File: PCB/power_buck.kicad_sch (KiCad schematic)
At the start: 6 parts

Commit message: fix: swap 3 JLCPCB-out-of-stock parts for in-stock equivalents
C_BAT1/C_BUCK_IN1/C_OLED_1/C_SYS_1/C_VIN_1 (10uF 0805 X5R 16V):
Yageo CC0805KRX5R7BB106 was at 0 stock -> HRE CGA0805X5R106K160MT
(LCSC C6119886, stock ~254k). Identical spec, different brand.

D_VBUS_TVS1: Nexperia PESD5V0S1BA,115 was down to 1 in stock -> TECH
PUBLIC TPPESD5V0S1BA (LCSC C587144, stock ~981k), a widely-stocked
pin/spec-compatible clone of the same part, same SOD-323 package.

Q_PWR1: Diodes Inc DMG2305UX-7 was down to 8 in stock -> Diodes Inc
DMG2305UX-13 (LCSC C144153, stock ~25k) -- same manufacturer, same
part, the -7/-13 suffix is just reel size (7"/13"), not an electrical
variant.

Found via live JLCPCB stock lookups after the JLCPCB upload flagged
these 3 with shortfalls. Verified via kicad-cli sch export bom and
sch erc (0 violations).

Note: PCB/snips_controller.kicad_pcb and the production/ exports still
need another Update-PCB-from-Schematic + Fabrication Toolkit pass to
pick up these changes -- not included here since they're a separate
manual step (see kicad_pcb_sync_gotcha note).

Co-Authored-By: Claude Sonnet 5 <noreply@anthropic.com>
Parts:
- C_BUCK_IN1: LCSC C2982567 -> C6119886; MF Yageo -> HRE; Manufacturer_Part_Number CC0805KRX5R7BB106 -> CGA0805X5R106K160MT
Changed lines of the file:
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@@
 			)
 		)
-		(property "MF" "Yageo"
+		(property "MF" "HRE"
 			(at 0 0 0)
 			(hide yes)
@@
 			)
 		)
-		(property "Manufacturer_Part_Number" "CC0805KRX5R7BB106"
+		(property "Manufacturer_Part_Number" "CGA0805X5R106K160MT"
 			(at 0 0 0)
 			(hide yes)
@@
 			)
 		)
-		(property "LCSC" "C2982567"
+		(property "LCSC" "C6119886"
 			(at 0 0 0)
 			(hide yes)

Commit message: task: alert on Basic-library alternatives during JLC part matching (#33)
* task: alert on Basic-library alternatives during JLC part matching

JLC's "Extended" library carries a per-unique-part setup fee on top of
unit price; "Basic" doesn't. That fee doesn't amortize well on a board
with many distinct low-quantity parts -- confirmed the hard way: our
first real JLCPCB assembly quote came back at $333.84 vs PCBWay's
~$190 for the same order, and all 33 of our matched parts were
Extended.

jlc_match.py now does a secondary search for a same-value/same-package
Basic-library part whenever the real match lands on Extended, and
flags it in the report (new BasicAlt column + a Status alert) rather
than silently leaving it. On the current board this surfaces 11
plausible Basic-library swaps (common resistor/cap values, and the
generic 1N4148W diode and 2N7002 MOSFET, which are industry-standard
parts many brands stock identically).

This is alert-only, same as the rest of this script -- it doesn't
touch the schematic. Spot-checked 4 of the 11 suggestions directly
against JLC's catalog to confirm value/package actually match, not
just a keyword hit.

Co-Authored-By: Claude Sonnet 5 <noreply@anthropic.com>

* fix: two correctness bugs in Basic-library alternative matching

1. find_basic_alternative() trusted the raw keyword-search hit without
   verifying the candidate's actual value -- JLC's fuzzy full-text search
   can return a wrong-value part that just shares digits (e.g. searching
   "100 0402" surfaced a 1kΩ resistor, EIA code "1001", as a false match
   for a 100Ω part). Now parses and compares the actual numeric value
   (with unit) before accepting a candidate; falls back to exact
   model-name matching for non-numeric values (generic diode/transistor
   part families like "1N4148W", "2N7002").

2. The new value parser's regex required the unit to be the first
   character of the string, but JLC resistor descriptions carry a
   Chinese prefix ("厚膜电阻 10kΩ ±1%" = "thi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
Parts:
- C_BUCK_IN1: LCSC C6119886 -> C15850; MF HRE -> Samsung Electro-Mechanics; Manufacturer_Part_Number CGA0805X5R106K160MT -> CL21A106KAYNNNE
- C_BUCK_OUT1: LCSC C76637 -> C45783; MF TDK -> Samsung Electro-Mechanics; Manufacturer_Part_Number C2012X5R1C226KT000E -> CL21A226MAQNNNE
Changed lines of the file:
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@@
 			)
 		)
-		(property "MF" "HRE"
+		(property "MF" "Samsung Electro-Mechanics"
 			(at 0 0 0)
 			(hide yes)
@@
 			)
 		)
-		(property "Manufacturer_Part_Number" "CGA0805X5R106K160MT"
+		(property "Manufacturer_Part_Number" "CL21A106KAYNNNE"
 			(at 0 0 0)
 			(hide yes)
@@
 			)
 		)
-		(property "LCSC" "C6119886"
+		(property "LCSC" "C15850"
 			(at 0 0 0)
 			(hide yes)
@@
 			)
 		)
-		(property "MF" "TDK"
+		(property "MF" "Samsung Electro-Mechanics"
 			(at 0 0 0)
 			(hide yes)
@@
 			)
 		)
-		(property "Manufacturer_Part_Number" "C2012X5R1C226KT000E"
+		(property "Manufacturer_Part_Number" "CL21A226MAQNNNE"
 			(at 0 0 0)
 			(hide yes)
@@
 			)
 		)
-		(property "LCSC" "C76637"
+		(property "LCSC" "C45783"
 			(at 0 0 0)
 			(hide yes)

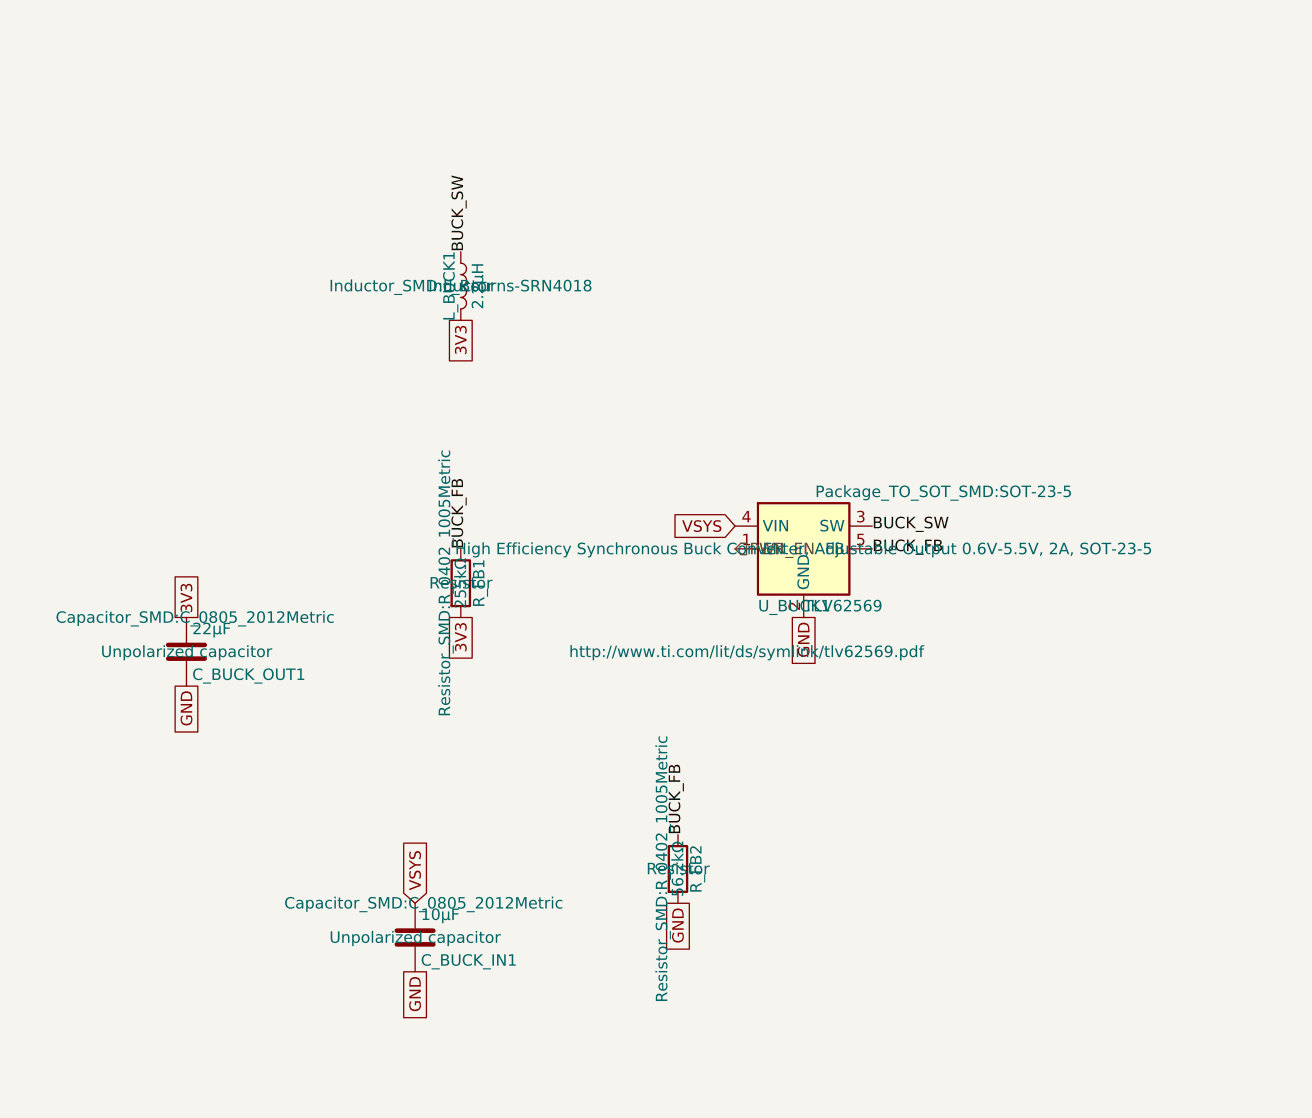
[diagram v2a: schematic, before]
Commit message: fix: make every BOM Value unambiguous for the fab, and switch D_INV_ISO1 to SOT-323 (#61)
* fix: make every BOM Value unambiguous for the fab, and switch D_INV_ISO1 to SOT-323

PCBWay flagged D_INV_ISO1: "BAT54W" is SOT-323 from nearly every maker, but we
had picked Yangjie's SOD-123 variant. A fab only sees Designator, Footprint,
Quantity and Value in the BOM (never MF/MPN/LCSC), so a bare part name is
ambiguous. Fixes the class of problem, not just this part:

- Every component's Value is now "<label> | <MPN> | <manufacturer> | <package>"
  (label dropped when it repeats the MPN; commas/periods stripped so the CSV
  never needs quoting). BT1 keeps its RIGHT-ANGLE HORIZONTAL note. Applied to
  all 81 parts across every sheet and the PCB.
- scripts/bom_values.py builds, applies, and checks these values, including
  that the PCB copy of Value/MF/MPN/footprint matches the schematic. New
  footprints must be added to its package table on purpose; hand-sourced parts
  with no MPN (J_STICK1) are listed explicitly.
- D_INV_ISO1 -> Diodes BAT54W-7-F in SOT-323 (common part, several makers).
  Pin 1 anode / pin 2 not connected / pin 3 cathode, confirmed against
  Nexperia's numbered pinning table and Diodes' datasheet. Uses KiCad's
  Diode:BAT54W symbol; PCB footprint replaced and rerouted. Electrically the
  same BAT54 family (30V, 200mA, 2uA leakage at 25V), so the SPICE model and
  scripts/spice/latch_sim.py still pass.
- Layout diagrams now say AO3401A for Q_PWR1 (they were stale since it was
  swapped from DMG2305UX) and BAT54W-7-F/SOT-323 for D_INV_ISO1.
- Repo CLAUDE.md documents the Value rule and the script.

ERC/DRC clean; production files regenerated.

Co-Authored-By: Claude Sonnet 5 <noreply@anthropic.com>

* chore: commit KiCad project settings (reordered used-designators list)

Co-Authored-By: Claude Sonnet 5 <noreply@anthropic.com>

---------

Co-authored-by: Claude Sonnet 5 <noreply@anthropic.com>
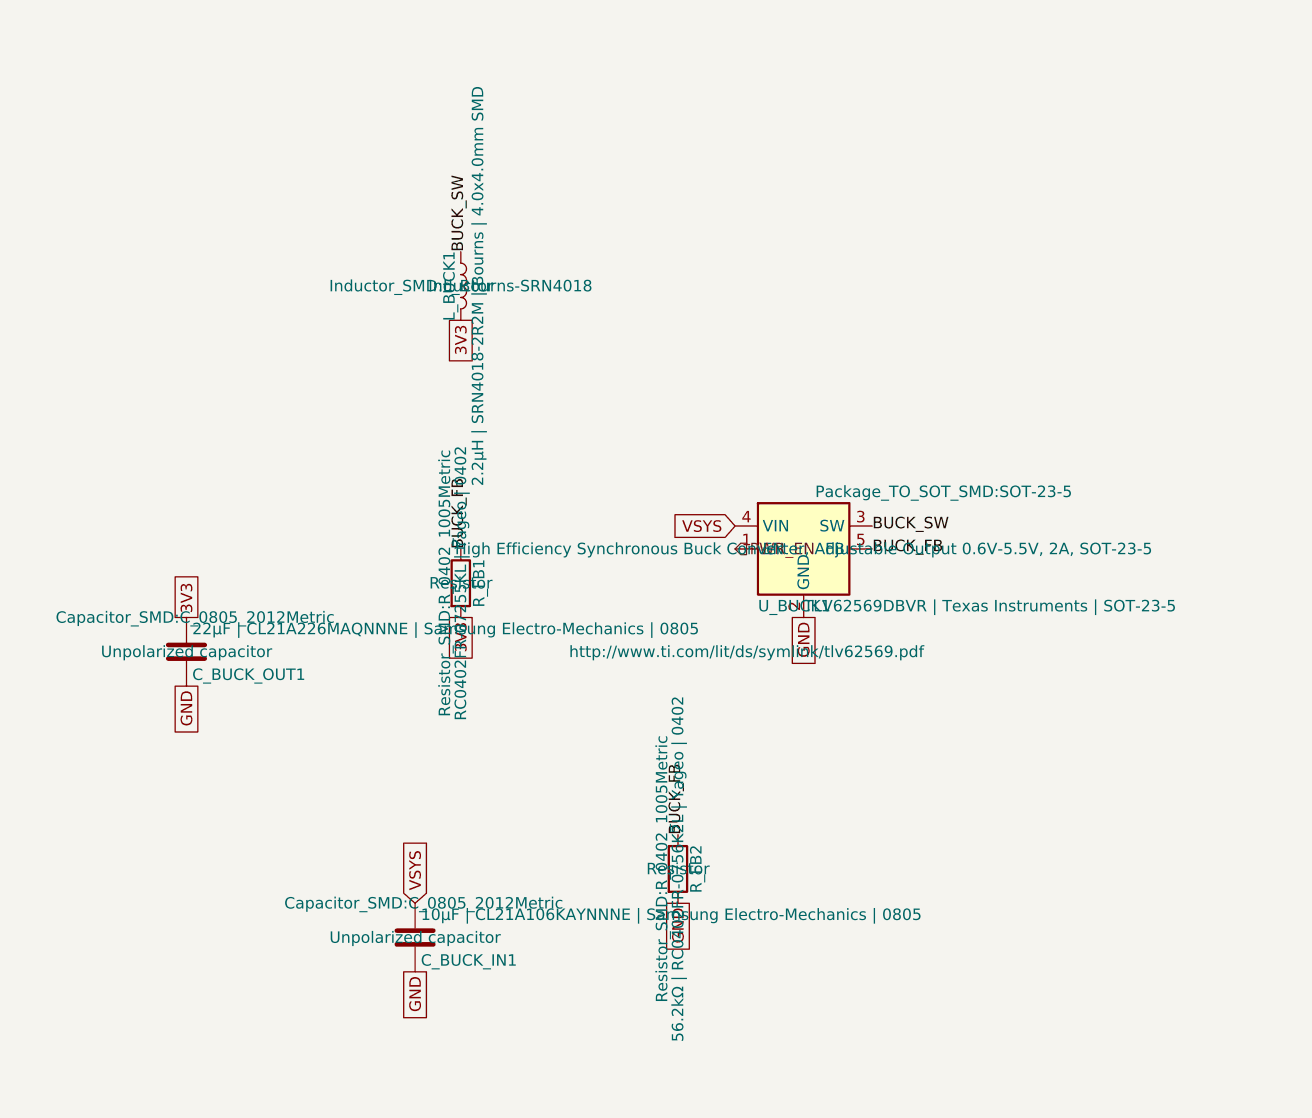
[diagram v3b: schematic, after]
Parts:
- C_BUCK_IN1: value 10µF -> 10µF | CL21A106KAYNNNE | Samsung Electro-Mechanics | 0805
- C_BUCK_OUT1: value 22µF -> 22µF | CL21A226MAQNNNE | Samsung Electro-Mechanics | 0805
- L_BUCK1: value 2.2µH -> 2.2µH | SRN4018-2R2M | Bourns | 4.0x4.0mm SMD
- R_FB1: value 255kΩ -> RC0402FR-07255KL | Yageo | 0402
- R_FB2: value 56.2kΩ -> 56.2kΩ | RC0402FR-0756K2L | Yageo | 0402
- U_BUCK1: value TLV62569 -> TLV62569DBVR | Texas Instruments | SOT-23-5
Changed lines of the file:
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@@
 			)
 		)
-		(property "Value" "255kΩ"
+		(property "Value" "RC0402FR-07255KL | Yageo | 0402"
 			(at 144.78 101.6 90)
 			(show_name no)
@@
 			)
 		)
-		(property "Value" "2.2µH"
+		(property "Value" "2.2µH | SRN4018-2R2M | Bourns | 4.0x4.0mm SMD"
 			(at 146.685 68.58 90)
 			(show_name no)
@@
 			)
 		)
-		(property "Value" "TLV62569"
+		(property "Value" "TLV62569DBVR | Texas Instruments | SOT-23-5"
 			(at 182.88 104.14 0)
 			(show_name no)
@@
 			)
 		)
-		(property "Value" "10µF"
+		(property "Value" "10µF | CL21A106KAYNNNE | Samsung Electro-Mechanics | 0805"
 			(at 140.335 138.43 0)
 			(show_name no)
@@
 			)
 		)
-		(property "Value" "22µF"
+		(property "Value" "22µF | CL21A226MAQNNNE | Samsung Electro-Mechanics | 0805"
 			(at 114.935 106.68 0)
 			(show_name no)
@@
 			)
 		)
-		(property "Value" "56.2kΩ"
+		(property "Value" "56.2kΩ | RC0402FR-0756K2L | Yageo | 0402"
 			(at 168.91 133.35 90)
 			(show_name no)
